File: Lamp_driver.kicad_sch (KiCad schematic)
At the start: 133 parts, among them J301 10146581-060_M, J302 T44007, J303 T44007, J304 10146581-060_M, J305 T44007, J306 T44007, Q301 MPF3N150, Q302 IXYH55N120, Q303 IXYH55N120, Q304 IXYH55N120, Q305 IXYH55N120, U301 IRS2184

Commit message: Added PCB
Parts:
- J301, J304: footprint Personal:Amphenol_Minitek_10146581-060_mod -> Personal:Amphenol_Minitek_10146581-060_mod_0
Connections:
- net Um_Lmp: now also C304.1, P346.1, R311.1, R313.2, TP307.1
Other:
- moved on the sheet: C303, C304, D310, R301, R302, R303, R304, R305, R306, R308, R309, R310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

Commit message: Readme updated
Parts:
- J301, J304: footprint Personal:Amphenol_Minitek_10146581-060_mod_0 -> Personal:Amphenol_Minitek_10146581-060_mod
- Q301: footprint Personal:To-220_staggered_2 -> Package_TO_SOT_THT:TO-220-3_Vertical

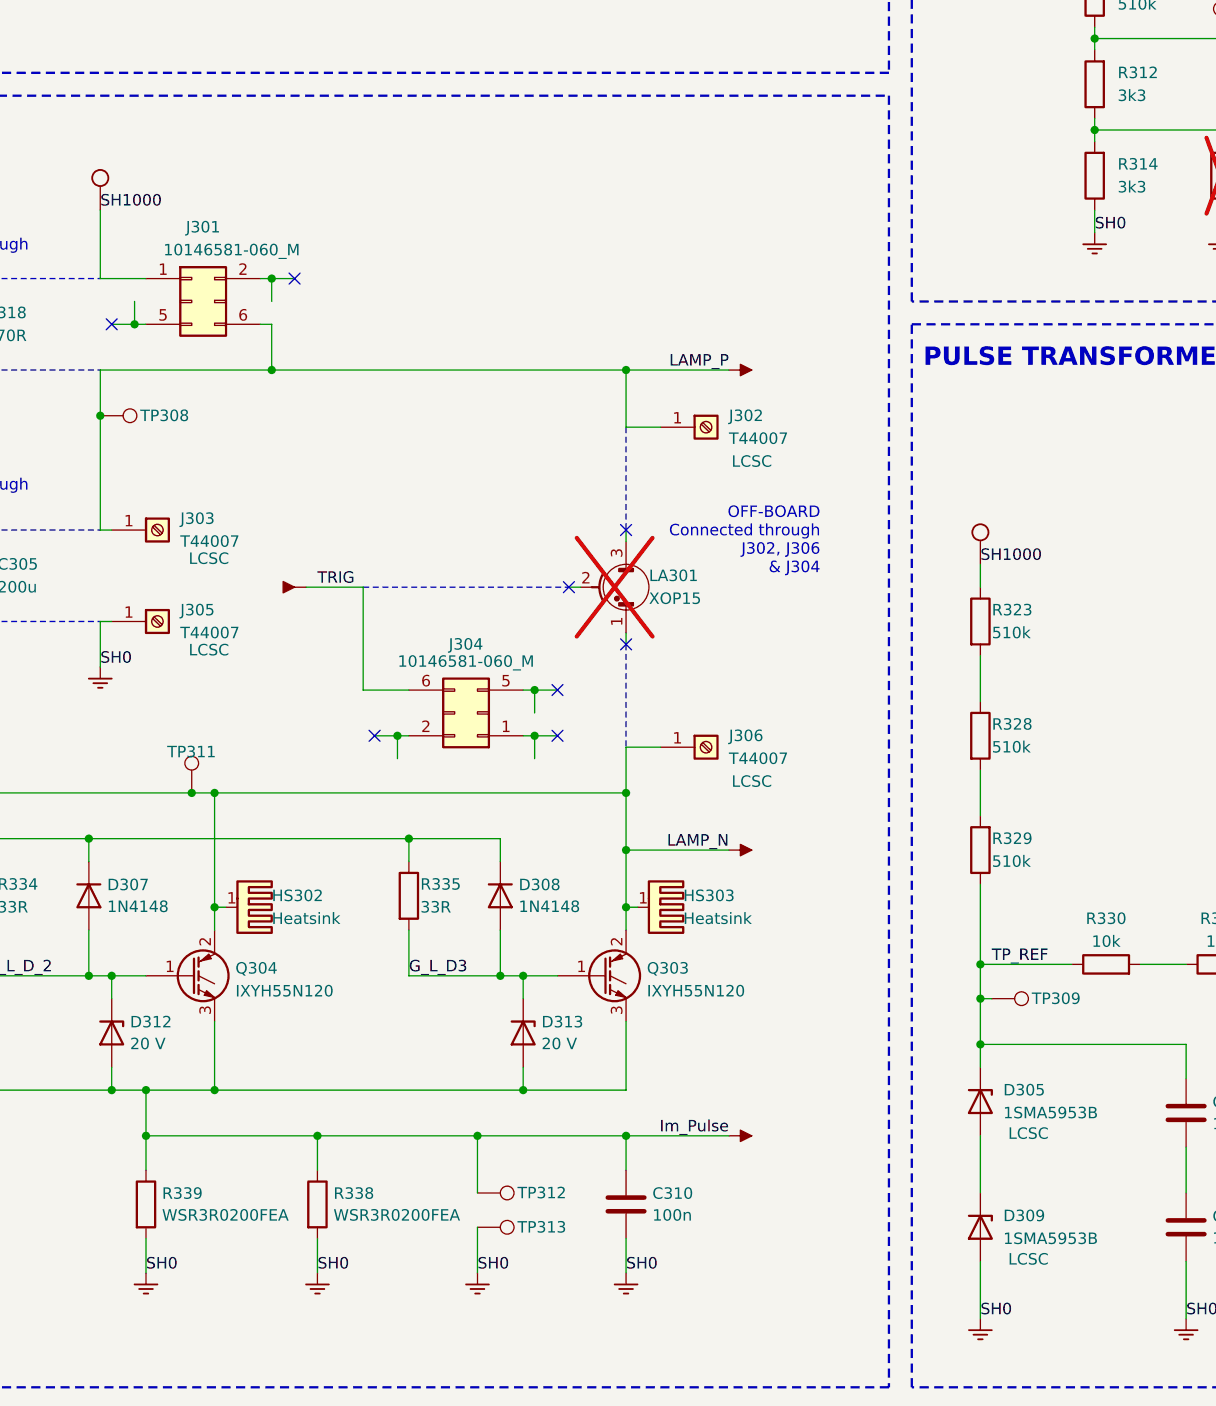
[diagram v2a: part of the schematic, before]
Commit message: updating BOM info
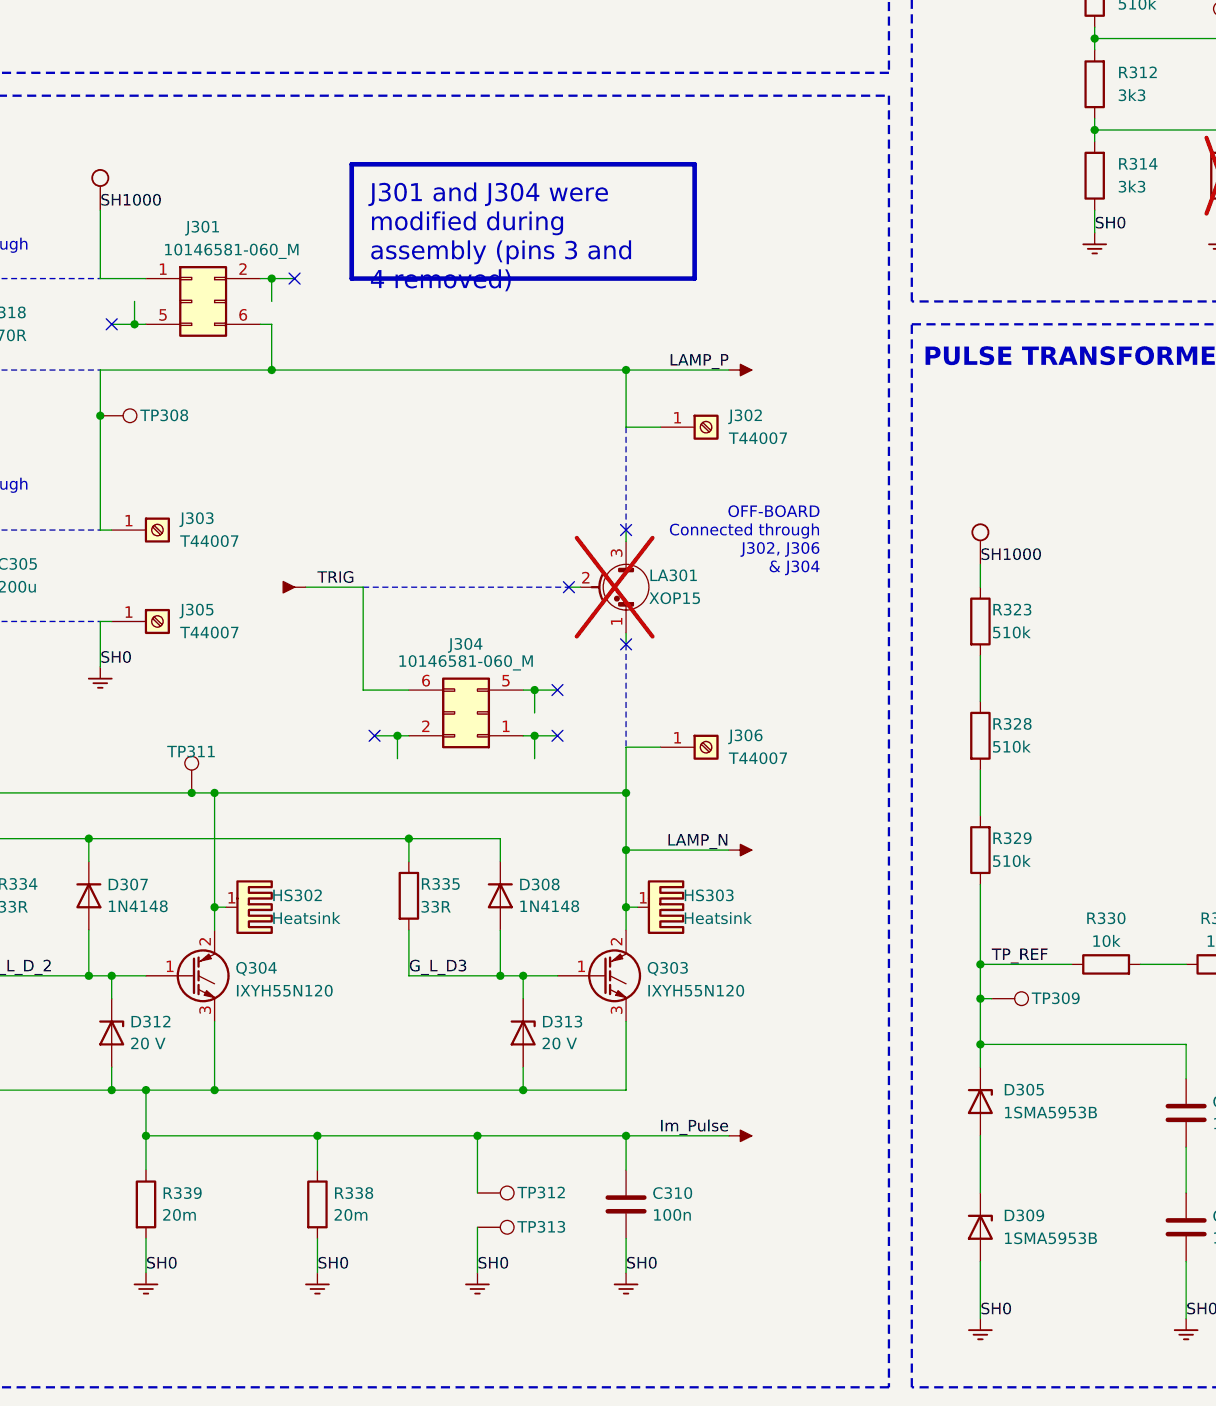
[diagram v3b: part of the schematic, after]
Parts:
- C301, C302, C303, C304, C310: Manufacturer (none) -> CCTC; Manufacturer Part Number (none) -> TCC0603X7R104K500CT
- C305, LA301: now in the parts list
- C307, C308, C309, R301, R302, R303, R304, R305, R306, R307, R308, R309, R310, R311, R312, R313, R314, R316, R323, R324, R325, R326, R327, R328, R329, R330, R331, R332, R333, R334, R335, R336, R337: Manufacturer (none) -> Generic
- D301, D302: Manufacturer (none) -> DIODES; Manufacturer Part Number (none) -> B360A-13-F
- D303, D310, D311, D312, D313: Manufacturer (none) -> HXY MOSFET; Manufacturer Part Number (none) -> BZT52C20
- D304: Field7 LCSC -> (none); Field8 https://lcsc.com/product-detail/Diodes-General-Purpose_LGE-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 -> (none); Manufacturer (none) -> LGE; Manufacturer Part Number (none) -> S15M
- D305, D309: Field5 LCSC -> (none); Manufacturer (none) -> Jingdao Microelectronics; Manufacturer Part Number (none) -> 1SMA5953B
- D306, D307, D308: Manufacturer (none) -> DIODES; Manufacturer Part Number (none) -> 1N4148W-7-F
- HS301, HS302, HS303: Link (none) -> https://www.aliexpress.com/item/32720811094.html?spm=a2g0o.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; Manufacturer (none) -> KY WIN ROBOT; Manufacturer Part Number (none) -> O-220 Heatsink
- J301, J304: Manufacturer (none) -> Amphenol; Manufacturer Part Number (none) -> 10146581-060
- J302, J303, J305, J306: Field5 https://lcsc.com/product-detail/PCB-Welding-Terminal_XFCN-T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 -> (none); Field6 LCSC -> (none); Manufacturer (none) -> XFCN; Manufacturer Part Number (none) -> T44007
- PT301: Manufacturer (none) -> Excelitas Technologies; Manufacturer Part Number (none) -> ZS1052-S_HT
- Q301: Manufacturer (none) -> C42401746; Manufacturer Part Number (none) -> MPF3N150
- Q302, Q303, Q304, Q305: Manufacturer (none) -> IXYS; Manufacturer Part Number (none) -> IXYH55N120
- R318: Field5 https://lcsc.com/product-detail/Through-Hole-Resistors_Huax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 -> (none); Link (none) -> https://lcsc.com/product-detail/Through-Hole-Resistors_Huax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; now in the parts list
- R338, R339: value WSR3R0200FEA -> 20m; Manufacturer (none) -> Vishay Intertech; Manufacturer Part Number (none) -> WSR3R0200FEA
- TP301, TP302, TP303, TP304, TP305, TP306, TP307, TP308, TP309, TP310, TP311, TP312, TP313: now left out of the parts list
- U301: Manufacturer (none) -> Infineon; Manufacturer Part Number (none) -> IRS2184

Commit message: Checked. Preparing release
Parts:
- J301, J304: footprint Personal:Amphenol_Minitek_10146581-060_mod -> Personal:Amphenol_Minitek_10146581-060_mod_0
- Q301: footprint Package_TO_SOT_THT:TO-220-3_Vertical -> Personal:To-220_staggered_2
- R337: value 2R2 -> 0
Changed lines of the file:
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@@
 			)
 		)
-		(property "Footprint" "Package_TO_SOT_THT:TO-220-3_Vertical"
+		(property "Footprint" "Personal:To-220_staggered_2"
 			(at 252.73 179.705 0)
 			(effects
@@
 			)
 		)
-		(property "Footprint" "Personal:Amphenol_Minitek_10146581-060_mod"
+		(property "Footprint" "Personal:Amphenol_Minitek_10146581-060_mod_0"
 			(at 136.398 155.194 0)
 			(effects
@@
 			)
 		)
-		(property "Footprint" "Personal:Amphenol_Minitek_10146581-060_mod"
+		(property "Footprint" "Personal:Amphenol_Minitek_10146581-060_mod_0"
 			(at 108.712 98.806 0)
 			(effects
@@
 			)
 		)
-		(property "Value" "2R2"
+		(property "Value" "0"
 			(at 39.37 189.23 90)
 			(effects

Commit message: Sch update in progress
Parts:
- removed HS301, HS302, HS303: Heatsink, Personal:Heatsink_26_16_40, symbol Mechanical:Heatsink_Pad
- removed J301: 10146581-060_M, Personal:Amphenol_Minitek_10146581-060_mod_0, symbol personal:Amphenol_Minitek_10146581-060_mod
- removed P348: ~, symbol personal:Cosmetic_GND
- removed P361: ~, symbol personal:Cosmetic_OUT
- removed P861: ~, symbol personal:Cosmetic_IN
- removed R318: 470R, Resistor_THT:R_Axial_Power_L50.0mm_W9.0mm_P55.88mm, symbol Device:R
- removed R325: 91k, Resistor_SMD:R_1206_3216Metric_Pad1.30x1.75mm_HandSolder, symbol Device:R
- removed R326, R327: 22k, Resistor_SMD:R_1206_3216Metric_Pad1.30x1.75mm_HandSolder, symbol Device:R
- removed TP302, TP303, TP304, TP305, TP306, TP307, TP312, TP313: TestPoint, TestPoint:TestPoint_THTPad_D1.0mm_Drill0.5mm, symbol Connector:TestPoint
- added P301, P302, P303, P304: ~, symbol personal:Cosmetic_GND
- added P305: ~, symbol personal:Cosmetic_PWR
- added R319: 100k, Resistor_SMD:R_0603_1608Metric_Pad0.98x0.95mm_HandSolder, symbol Device:R
- added TP302, TP303, TP304, TP312, TP313: Testpoint_osc_probe, Personal:Testpoint_osc_no_lead, symbol personal:OscTestpoint
- R323, R328, R329: value 510k -> 330k
- R324: value 91k -> 100k; footprint Resistor_SMD:R_1206_3216Metric_Pad1.30x1.75mm_HandSolder -> Resistor_THT:R_Axial_DIN0617_L17.0mm_D6.0mm_P5.08mm_Vertical
- R330, R331: value 10k -> 110k
- R333, R334, R335: value 33R -> 91R
- R337: value 0 -> 22R; footprint Resistor_SMD:R_0603_1608Metric_Pad0.98x0.95mm_HandSolder -> Resistor_SMD:R_1206_3216Metric_Pad1.30x1.75mm_HandSolder
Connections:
- net SH1000 is gone; now on net S1k: P351.1, P362.1, P363.1, P794.1, R323.1, R324.1
- net DRV_OUT: now also D306.2 (A), D307.2 (A), D308.2 (A), TP313.1 (Sig); no longer D306.1 (K), D307.1 (K), D308.1 (K)
- net G_L_D1: now also D306.1 (K); no longer D306.2 (A)
- net G_L_D3: now also D308.1 (K); no longer D308.2 (A)
- net G_L_D_2: now also D307.1 (K); no longer D307.2 (A)
- net G_TP_REF: now also R319.1
- net SH0: now also P301.1, P302.1, P303.1, P304.1, TP302.2 (Ref), TP303.2 (Ref), TP304.2 (Ref), TP312.2 (Ref), TP313.2 (Ref)
- net TP_DRV_COL: now also R324.2
- net TP_PRI: now also R319.2
- net at D305.2 (A), D309.1 (K): now also C307.2, C309.1
- net Im_Pulse renamed Mon_IL
- net Mon_IL: now also TP312.1 (Sig)
- net LAMP_N renamed LMP
- net LAMP_P renamed S1k
- net S1k: now also P305.1
- net Lamp_EN renamed LMP_EN
- net LMP_EN: now also TP302.1 (Sig)
- net Um_Col renamed Mon_LMP
- net Mon_LMP: now also TP303.1 (Sig)
- net Um_Lmp renamed Mon_S1k
- net Mon_S1k: now also TP304.1 (Sig)
- no-connect marks 14 -> 10
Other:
- note removed: "OFF-BOARD Connected through J301"
- moved on the sheet: C308, D303, D306, D307, D308, Q301, R324

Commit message: Placement 50%
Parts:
- removed P354, P357: ~, symbol personal:Cosmetic_GND
- removed R302, R304: NF, Resistor_SMD:R_1206_3216Metric_Pad1.30x1.75mm_HandSolder, symbol Device:R
- removed R315, R317: NF, Resistor_SMD:R_0603_1608Metric_Pad0.98x0.95mm_HandSolder, symbol Device:R
- removed TP301: TestPoint, TestPoint:TestPoint_THTPad_D1.0mm_Drill0.5mm, symbol Connector:TestPoint
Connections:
- net TP_COM: now also D304.2 (A); no longer R332.1
- net TP_PRI: now also R332.2; no longer D304.1 (K)
- new net: D304.1 (K), R332.1
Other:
- moved on the sheet: C303, C304, D304, R301, R303, R305, R306, R308, R309, R310, R311, R312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

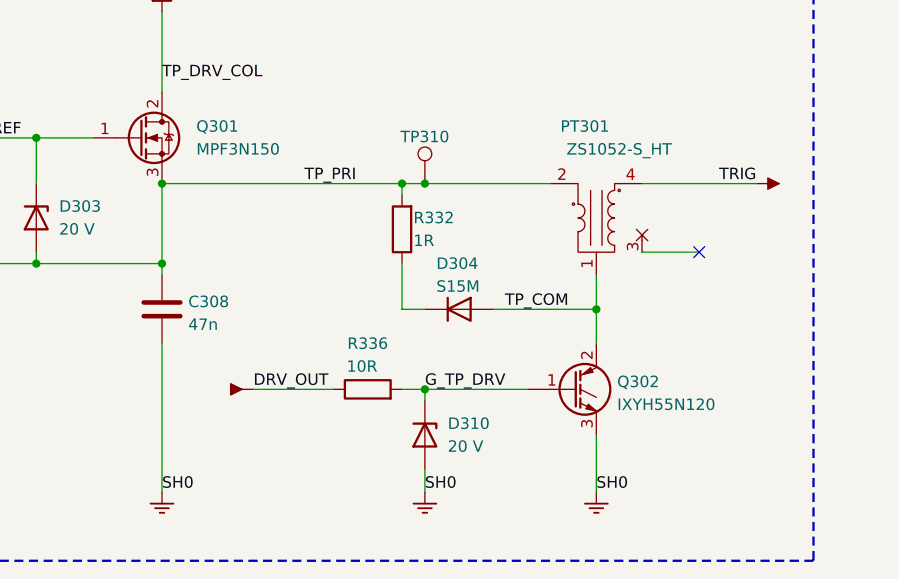
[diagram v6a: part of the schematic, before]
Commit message: Updated pulse transofrmer circuit
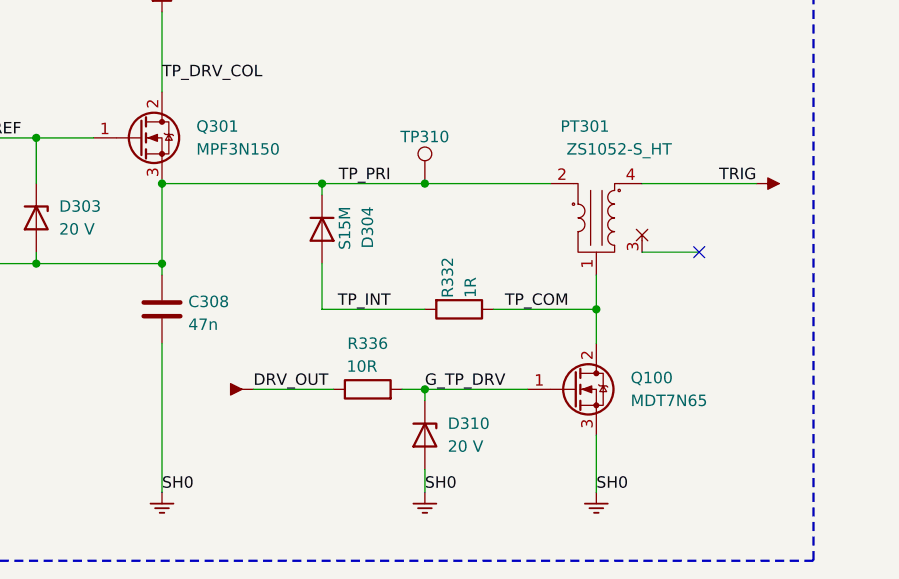
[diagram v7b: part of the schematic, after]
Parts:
- removed Q302: IXYH55N120, Personal:TO-247_small_p1, symbol Device:Q_NIGBT_GCE
- added Q100: MDT7N65, Package_TO_SOT_SMD:TO-252-2, symbol Transistor_FET:BUZ11
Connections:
- net G_TP_DRV: now also Q100.1 (G)
- net SH0: now also Q100.3 (S)
- net TP_COM: now also R332.1, Q100.2 (D); no longer D304.2 (A)
- net TP_PRI: now also D304.1 (K); no longer R332.2
- new net TP_INT: D304.2 (A), R332.2
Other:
- moved on the sheet: D304, R332

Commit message: Placement updates
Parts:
- added P137: ~, symbol personal:Cosmetic_IN
- added P138: ~, symbol personal:Cosmetic_GND
- added R102: 10R, Resistor_SMD:R_1206_3216Metric_Pad1.30x1.75mm_HandSolder, symbol Device:R
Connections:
- net DRV_RET: now also P137.1, R102.1
- net SH0: now also P138.1, R102.2
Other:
- moved on the sheet: D304, D310, PT301, Q100, R332, R336, TP310
